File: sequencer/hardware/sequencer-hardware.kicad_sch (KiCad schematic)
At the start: 53 parts, among them J1 Barrel Jack, J2 40Pin 0.1", J3 USB_B_Micro, J4 Conn_01x02_Male, J5 JST 4-Pin male, J6 TS Out, SW1 PWR, SW2 SW_Push, U1 L7805_A, U2 L7805_D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

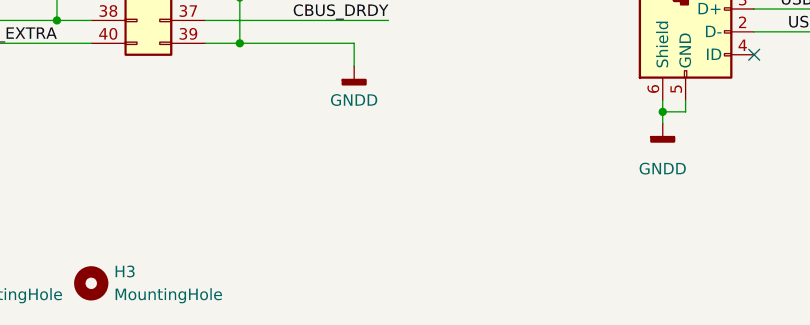
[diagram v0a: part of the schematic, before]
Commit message: Add ground planes
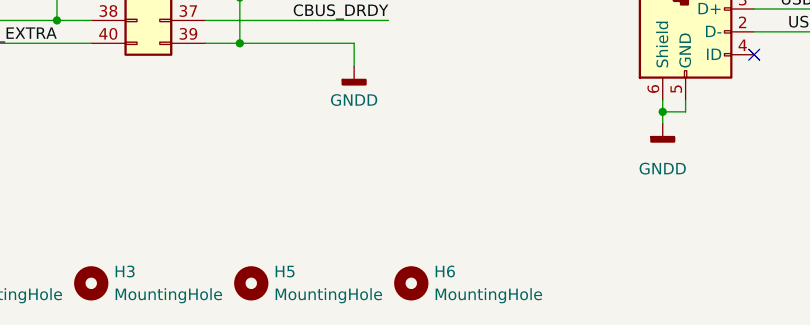
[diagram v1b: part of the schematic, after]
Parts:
- added H5, H6: MountingHole, MountingHole:MountingHole_3.2mm_M3_ISO14580, symbol Mechanical:MountingHole
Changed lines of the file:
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@@
     (pin "2")
+  )
+  (symbol (lib_id "Mechanical:MountingHole") (at 87.63 199.39 0) (unit 1)
+    (in_bom yes) (on_board yes) (fields_autoplaced)
+    (property "Reference" "H6" (id 0) (at 90.17 198.1199 0)
+      (effects (font (size 1.27 1.27)) (justify left))
+    )
+    (property "Value" "MountingHole" (id 1) (at 90.17 200.6599 0)
+      (effects (font (size 1.27 1.27)) (justify left))
+    )
+    (property "Footprint" "MountingHole:MountingHole_3.2mm_M3_ISO14580" (id 2) (at 87.63 199.39 0)
+      (effects (font (size 1.27 1.27)) hide)
+    )
+    (property "Datasheet" "~" (id 3) (at 87.63 199.39 0)
+      (effects (font (size 1.27 1.27)) hide)
+    )
   )
   (symbol (lib_name "OPAMP_1") (lib_id "pspice:OPAMP") (at 281.94 138.43 0) (mirror x) (unit 1)
@@
     (pin "7")
     (pin "8")
+  )
+  (symbol (lib_id "Mechanical:MountingHole") (at 69.85 199.39 0) (unit 1)
+    (in_bom yes) (on_board yes) (fields_autoplaced)
+    (property "Reference" "H5" (id 0) (at 72.39 198.1199 0)
+      (effects (font (size 1.27 1.27)) (justify left))
+    )
+    (property "Value" "MountingHole" (id 1) (at 72.39 200.6599 0)
+      (effects (font (size 1.27 1.27)) (justify left))
+    )
+    (property "Footprint" "MountingHole:MountingHole_3.2mm_M3_ISO14580" (id 2) (at 69.85 199.39 0)
+      (effects (font (size 1.27 1.27)) hide)
+    )
+    (property "Datasheet" "~" (id 3) (at 69.85 199.39 0)
+      (effects (font (size 1.27 1.27)) hide)
+    )
   )
   (symbol (lib_id "Filter:Choke_Schaffner_RN102-2-02-1M1") (at 36.83 40.64 0) (unit 1)
@@
       (reference "H4") (unit 1) (value "MountingHole") (footprint "MountingHole:MountingHole_3.2mm_M3_ISO14580_Pad")
     )
+    (path "/6ae32483-2b45-48a6-a7ab-d54762dd8df9"
+      (reference "H5") (unit 1) (value "MountingHole") (footprint "MountingHole:MountingHole_3.2mm_M3_ISO14580")
+    )
+    (path "/03befa8e-af78-4112-87b1-19a6aed29f7f"
+      (reference "H6") (unit 1) (value "MountingHole") (footprint "MountingHole:MountingHole_3.2mm_M3_ISO14580")
+    )
     (path "/e7d77e35-7d0f-418c-bddb-e70c65e01157"
       (reference "J1") (unit 1) (value "Barrel Jack") (footprint "Connector_BarrelJack:BarrelJack_Horizontal")
@@
       (reference "R37") (unit 1) (value "1k") (footprint "Resistor_SMD:R_0603_1608Metric_Pad0.98x0.95mm_HandSolder")
     )
+    (path "/56dcffd5-e973-4f89-956d-68b94266f270/0809c410-6284-4664-9ee1-586a66288ddc"
+      (reference "R38") (unit 1) (value "10k") (footprint "Resistor_SMD:R_0603_1608Metric_Pad0.98x0.95mm_HandSolder")
+    )
+    (path "/56dcffd5-e973-4f89-956d-68b94266f270/aa415fd7-5826-4c58-b1af-9ca95b3ef519"
+      (reference "R39") (unit 1) (value "10k") (footprint "Resistor_SMD:R_0603_1608Metric_Pad0.98x0.95mm_HandSolder")
+    )
     (path "/2cc3a222-efe9-400d-8ec9-be9ab26a505c"

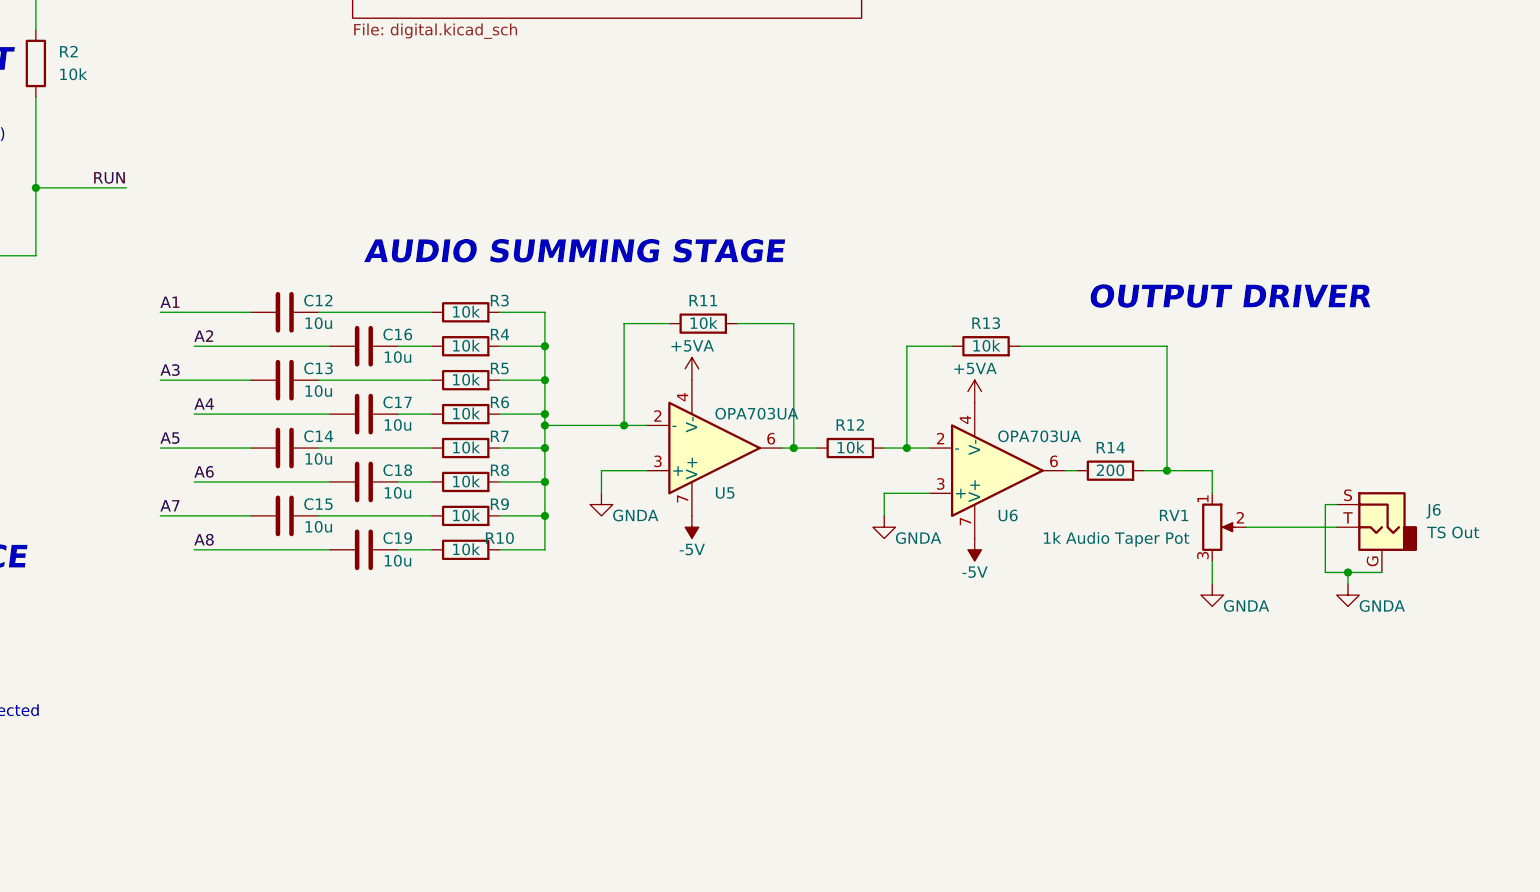
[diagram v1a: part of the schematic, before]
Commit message: Route analog domain
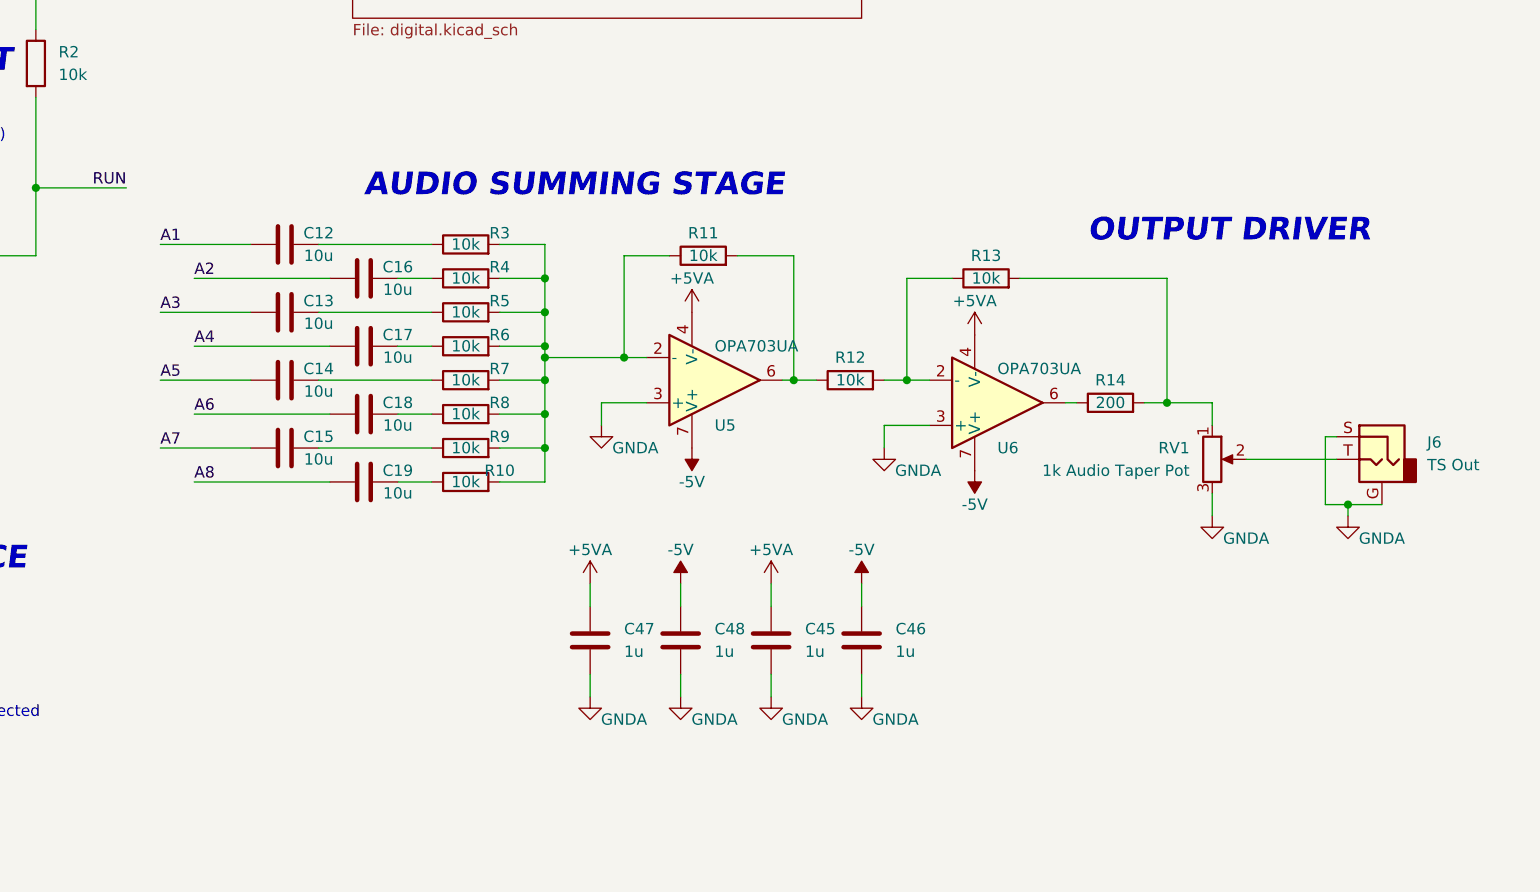
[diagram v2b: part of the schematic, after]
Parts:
- added C45, C46, C47, C48: 1u, Capacitor_SMD:C_0603_1608Metric_Pad1.08x0.95mm_HandSolder, symbol Device:C
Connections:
- net +5VA: now also C45.1, C47.1
- net -5V: now also C46.1, C48.1
- net GNDA: now also C45.2, C46.2, C47.2, C48.2
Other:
- moved on the sheet: C12, C13, C14, C15, C16, C17, C18, C19, J6, R10, R11, R12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

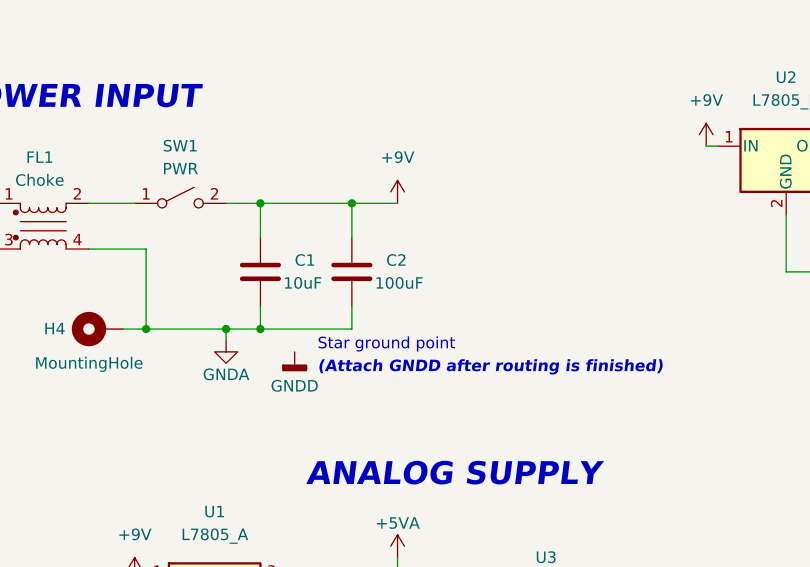
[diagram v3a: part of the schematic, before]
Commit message: Cleanup silkscreen
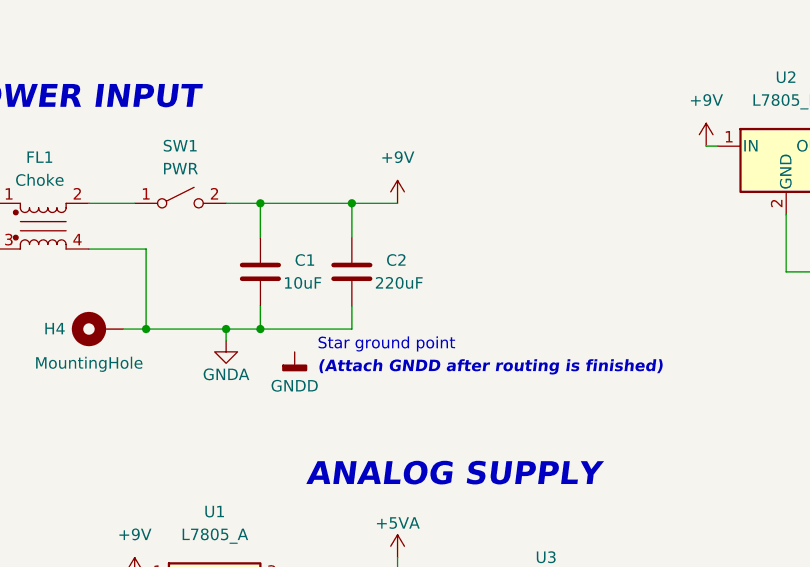
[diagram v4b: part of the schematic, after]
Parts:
- C2: value 100uF -> 220uF
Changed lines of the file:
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@@
       (effects (font (size 1.27 1.27)) (justify left))
     )
-    (property "Value" "100uF" (id 1) (at 73.66 46.99 0)
+    (property "Value" "220uF" (id 1) (at 73.66 46.99 0)
       (effects (font (size 1.27 1.27)) (justify left))
     )
@@
     )
     (path "/71bcca76-dcd0-45b6-a387-efe1c2713601"
-      (reference "C2") (unit 1) (value "100uF") (footprint "Capacitor_THT:CP_Radial_D8.0mm_P3.50mm")
+      (reference "C2") (unit 1) (value "220uF") (footprint "Capacitor_THT:CP_Radial_D8.0mm_P3.50mm")
     )
     (path "/e263c6c9-245b-49e7-9320-f31d739535dc"

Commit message: Add star ground point
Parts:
- added JP1: SolderJumper_2_Bridged, custom:SolderJumper-2_P1.3mm_Bridged_Pad1.0x1.5mm, symbol Jumper:SolderJumper_2_Bridged
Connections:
- net GNDA: now also JP1.1 (A)
- net GNDD: now also JP1.2 (B)
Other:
- note removed: "(Attach GNDD after routing is finished)"
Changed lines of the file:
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@@
   (junction (at 231.14 116.84) (diameter 0) (color 0 0 0 0)
   )
+  (junction (at 62.23 52.07) (diameter 0) (color 0 0 0 0)
+  )
   (junction (at 48.26 170.18) (diameter 0) (color 0 0 0 0)
   )
@@
   (junction (at 68.58 157.48) (diameter 0) (color 0 0 0 0)
   )
+  (junction (at 52.07 52.07) (diameter 0) (color 0 0 0 0)
+  )
   (junction (at 135.89 31.75) (diameter 0) (color 0 0 0 0)
   )
@@
   (junction (at 72.39 80.01) (diameter 0) (color 0 0 0 0)
   )
-  (junction (at 146.05 31.75) (diameter 0) (color 0 0 0 0)
-  )
   (junction (at 231.14 135.89) (diameter 0) (color 0 0 0 0)
   )
@@
   (junction (at 68.58 172.72) (diameter 0) (color 0 0 0 0)
   )
+  (junction (at 66.04 38.1) (diameter 0) (color 0 0 0 0)
+  )
   (no_connect (at 90.17 107.95))
   (no_connect (at 52.07 157.48))
@@
     (stroke (width 0) (type default) (color 0 0 0 0))
   )
+  (wire (pts (xy 66.04 35.56) (xy 66.04 38.1))
+    (stroke (width 0) (type default) (color 0 0 0 0))
+  )
   (wire (pts (xy 71.12 52.07) (xy 71.12 49.53))
     (stroke (width 0) (type default) (color 0 0 0 0))
@@
     (stroke (width 0) (type default) (color 0 0 0 0))
   )
+  (wire (pts (xy 66.04 38.1) (xy 71.12 38.1))
+    (stroke (width 0) (type default) (color 0 0 0 0))
+  )
   (wire (pts (xy 35.56 124.46) (xy 52.07 124.46))
     (stroke (width 0) (type default) (color 0 0 0 0))
@@
     (stroke (width 0) (type default) (color 0 0 0 0))
   )
+  (polyline (pts (xy 76.2 51.435) (xy 62.865 51.435))
+    (stroke (width 0) (type default) (color 0 0 0 0))
+  )
   (wire (pts (xy 135.89 31.75) (xy 135.89 35.56))
     (stroke (width 0) (type default) (color 0 0 0 0))
@@
     (stroke (width 0) (type default) (color 0 0 0 0))
   )
-  (wire (pts (xy 60.96 52.07) (xy 71.12 52.07))
+  (wire (pts (xy 60.96 52.07) (xy 62.23 52.07))
     (stroke (width 0) (type default) (color 0 0 0 0))
   )
@@
     (stroke (width 0) (type default) (color 0 0 0 0))
   )
-  (wire (pts (xy 135.89 31.75) (xy 146.05 31.75))
+  (wire (pts (xy 135.89 31.75) (xy 151.13 31.75))
     (stroke (width 0) (type default) (color 0 0 0 0))
   )
@@
     (stroke (width 0) (type default) (color 0 0 0 0))
   )
-  (wire (pts (xy 146.05 27.94) (xy 146.05 31.75))
-    (stroke (width 0) (type default) (color 0 0 0 0))
-  )
   (wire (pts (xy 102.87 88.9) (xy 105.41 88.9))
     (stroke (width 0) (type default) (color 0 0 0 0))
@@
     (stroke (width 0) (type default) (color 0 0 0 0))
   )
+  (wire (pts (xy 62.23 54.61) (xy 62.23 52.07))
+    (stroke (width 0) (type default) (color 0 0 0 0))
+  )
   (wire (pts (xy 80.01 88.9) (xy 80.01 90.17))
     (stroke (width 0) (type default) (color 0 0 0 0))
@@
     (stroke (width 0) (type default) (color 0 0 0 0))
   )
-  (wire (pts (xy 48.26 52.07) (xy 57.15 52.07))
+  (wire (pts (xy 48.26 52.07) (xy 52.07 52.07))
     (stroke (width 0) (type default) (color 0 0 0 0))
   )
@@
     (stroke (width 0) (type default) (color 0 0 0 0))
   )
+  (wire (pts (xy 64.77 54.61) (xy 62.23 54.61))
+    (stroke (width 0) (type default) (color 0 0 0 0))
+  )
   (wire (pts (xy 119.38 45.72) (xy 128.27 45.72))
     (stroke (width 0) (type default) (color 0 0 0 0))
@@
     (stroke (width 0) (type default) (color 0 0 0 0))
   )
-  (wire (pts (xy 146.05 31.75) (xy 151.13 31.75))
-    (stroke (width 0) (type default) (color 0 0 0 0))
-  )
   (wire (pts (xy 48.26 160.02) (xy 48.26 165.1))
     (stroke (width 0) (type default) (color 0 0 0 0))
@@
     (stroke (width 0) (type default) (color 0 0 0 0))
   )
+  (wire (pts (xy 72.39 54.61) (xy 74.93 54.61))
+    (stroke (width 0) (type default) (color 0 0 0 0))
+  )
   (wire (pts (xy 81.28 175.26) (xy 81.28 172.72))
     (stroke (width 0) (type default) (color 0 0 0 0))
@@
     (stroke (width 0) (type default) (color 0 0 0 0))
   )
+  (wire (pts (xy 74.93 54.61) (xy 74.93 57.15))
+    (stroke (width 0) (type default) (color 0 0 0 0))
+  )
   (wire (pts (xy 226.06 116.84) (xy 231.14 116.84))
     (stroke (width 0) (type default) (color 0 0 0 0))
   )
-  (wire (pts (xy 60.96 38.1) (xy 71.12 38.1))
+  (wire (pts (xy 60.96 38.1) (xy 66.04 38.1))
     (stroke (width 0) (type default) (color 0 0 0 0))
   )
@@
     (stroke (width 0) (type default) (color 0 0 0 0))
   )
+  (wire (pts (xy 52.07 52.07) (xy 57.15 52.07))
+    (stroke (width 0) (type default) (color 0 0 0 0))
+  )
   (wire (pts (xy 135.89 45.72) (xy 135.89 43.18))
     (stroke (width 0) (type default) (color 0 0 0 0))
@@
     (stroke (width 0) (type default) (color 0 0 0 0))
   )
+  (wire (pts (xy 52.07 52.07) (xy 52.07 54.61))
+    (stroke (width 0) (type default) (color 0 0 0 0))
+  )
   (wire (pts (xy 76.2 77.47) (xy 76.2 80.01))
     (stroke (width 0) (type default) (color 0 0 0 0))
@@
     (stroke (width 0) (type default) (color 0 0 0 0))
   )
+  (polyline (pts (xy 62.865 51.435) (xy 62.865 50.8))
+    (stroke (width 0) (type default) (color 0 0 0 0))
+  )
   (wire (pts (xy 68.58 157.48) (xy 68.58 162.56))
     (stroke (width 0) (type default) (color 0 0 0 0))
   )
+  (polyline (pts (xy 62.865 50.8) (xy 63.5 50.8))
+    (stroke (width 0) (type default) (color 0 0 0 0))
+  )
   (wire (pts (xy 226.06 113.03) (xy 231.14 113.03))
     (stroke (width 0) (type default) (color 0 0 0 0))
@@
     (stroke (width 0) (type default) (color 0 0 0 0))
   )
+  (wire (pts (xy 62.23 52.07) (xy 71.12 52.07))
+    (stroke (width 0) (type default) (color 0 0 0 0))
+  )
   (wire (pts (xy 231.14 139.7) (xy 231.14 135.89))
     (stroke (width 0) (type default) (color 0 0 0 0))
@@
     (stroke (width 0) (type default) (color 0 0 0 0))
   )
-  (text "(Attach GNDD after routing is finished)" (at 67.31 57.15 0)
-    (effects (font (size 1.27 1.27) (thickness 0.254) bold italic) (justify left bottom))
-  )
   (text "OUTPUT DRIVER" (at 292.1 113.03 0)
     (effects (font (size 2.54 2.54) (thickness 0.508) bold italic) (justify left bottom))
@@
     (effects (font (size 2.54 2.54) (thickness 0.508) bold italic) (justify left bottom))
   )
-  (text "Star ground point" (at 67.31 54.61 0)
+  (text "Star ground point" (at 77.47 52.07 0)
     (effects (font (size 1.27 1.27)) (justify left bottom))
   )
@@
     (pin "2")
   )
+  (symbol (lib_id "Jumper:SolderJumper_2_Bridged") (at 68.58 54.61 0) (unit 1)
+    (in_bom yes) (on_board yes)
+    (property "Reference" "JP1" (id 0) (at 68.58 57.15 0))
+    (property "Value" "SolderJumper_2_Bridged" (id 1) (at 85.09 53.34 0)
+      (effects (font (size 1.27 1.27)) hide)
+    )
+    (property "Footprint" "custom:SolderJumper-2_P1.3mm_Bridged_Pad1.0x1.5mm" (id 2) (at 68.58 54.61 0)
+      (effects (font (size 1.27 1.27)) hide)
+    )
+    (property "Datasheet" "~" (id 3) (at 68.58 54.61 0)
+      (effects (font (size 1.27 1.27)) hide)
+    )
+    (pin "1")
+    (pin "2")
+  )
   (symbol (lib_id "Device:C") (at 201.93 128.27 90) (unit 1)
     (in_bom yes) (on_board yes)
@@
     )
   )
+  (symbol (lib_id "power:PWR_FLAG") (at 52.07 54.61 180) (unit 1)
+    (in_bom yes) (on_board yes)
+    (property "Reference" "#FLG0101" (id 0) (at 52.07 56.515 0)
+      (effects (font (size 1.27 1.27)) hide)
+    )
+    (property "Value" "PWR_FLAG" (id 1) (at 46.99 59.69 0)
+      (effects (font (size 1.27 1.27)) (justify right))
+    )
+    (property "Footprint" "" (id 2) (at 52.07 54.61 0)
+      (effects (font (size 1.27 1.27)) hide)
+    )
+    (property "Datasheet" "~" (id 3) (at 52.07 54.61 0)
+      (effects (font (size 1.27 1.27)) hide)
+    )
+    (pin "1")
+  )
   (symbol (lib_id "power:+5VA") (at 256.54 151.13 0) (unit 1)
     (in_bom yes) (on_board yes)
@@
     (pin "2")
   )
-  (symbol (lib_id "power:PWR_FLAG") (at 146.05 27.94 0) (unit 1)
+  (symbol (lib_id "power:PWR_FLAG") (at 66.04 35.56 0) (unit 1)
     (in_bom yes) (on_board yes) (fields_autoplaced)
-    (property "Reference" "#FLG01" (id 0) (at 146.05 26.035 0)
+    (property "Reference" "#FLG01" (id 0) (at 66.04 33.655 0)
       (effects (font (size 1.27 1.27)) hide)
     )
-    (property "Value" "PWR_FLAG" (id 1) (at 146.05 22.86 0))
-    (property "Footprint" "" (id 2) (at 146.05 27.94 0)
+    (property "Value" "PWR_FLAG" (id 1) (at 66.04 30.48 0))
+    (property "Footprint" "" (id 2) (at 66.04 35.56 0)
       (effects (font (size 1.27 1.27)) hide)
     )
-    (property "Datasheet" "~" (id 3) (at 146.05 27.94 0)
+    (property "Datasheet" "~" (id 3) (at 66.04 35.56 0)
       (effects (font (size 1.27 1.27)) hide)
     )
@@
     (pin "9")
   )
-  (symbol (lib_id "power:GNDD") (at 64.77 54.61 0) (unit 1)
+  (symbol (lib_id "power:GNDD") (at 74.93 57.15 0) (unit 1)
     (in_bom yes) (on_board yes)
-    (property "Reference" "#PWR08" (id 0) (at 64.77 60.96 0)
+    (property "Reference" "#PWR08" (id 0) (at 74.93 63.5 0)
       (effects (font (size 1.27 1.27)) hide)
     )
-    (property "Value" "GNDD" (id 1) (at 64.77 58.42 0))
-    (property "Footprint" "" (id 2) (at 64.77 54.61 0)
+    (property "Value" "GNDD" (id 1) (at 74.93 60.96 0))
+    (property "Footprint" "" (id 2) (at 74.93 57.15 0)
       (effects (font (size 1.27 1.27)) hide)
     )
-    (property "Datasheet" "" (id 3) (at 64.77 54.61 0)
+    (property "Datasheet" "" (id 3) (at 74.93 57.15 0)
       (effects (font (size 1.27 1.27)) hide)
     )
@@
       (reference "#FLG01") (unit 1) (value "PWR_FLAG") (footprint "")
     )
+    (path "/6be5609b-fe8c-49cb-a6f3-dcd349ebdab6"
+      (reference "#FLG0101") (unit 1) (value "PWR_FLAG") (footprint "")
+    )
     (path "/82306ab4-f7d3-4833-8f9e-b2e7e7bdcf50"
       (reference "#PWR01") (unit 1) (value "+5VD") (footprint "")
@@
       (reference "J17") (unit 1) (value "Conn_01x03") (footprint "Connector_PinHeader_2.54mm:PinHeader_1x03_P2.54mm_Vertical")
     )
+    (path "/4db95d31-7cd6-425a-aba5-1ff58537d849"
+      (reference "JP1") (unit 1) (value "SolderJumper_2_Bridged") (footprint "custom:SolderJumper-2_P1.3mm_Bridged_Pad1.0x1.5mm")
+    )
     (path "/d1178891-9012-4ece-af80-f2acf0ed95f0"
